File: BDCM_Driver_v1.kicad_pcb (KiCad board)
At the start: 4 copper layers, 32 x 33 mm, 38 parts, among them J1 OUT_{A}, J2 Encoder, J3 ST-Link, J4 Power, J5 I^{2}C, J6 Encoder, J7 OUT_{B}, SW1 RST, U1 STM32C011F4Px, U2 TB67H450FNG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

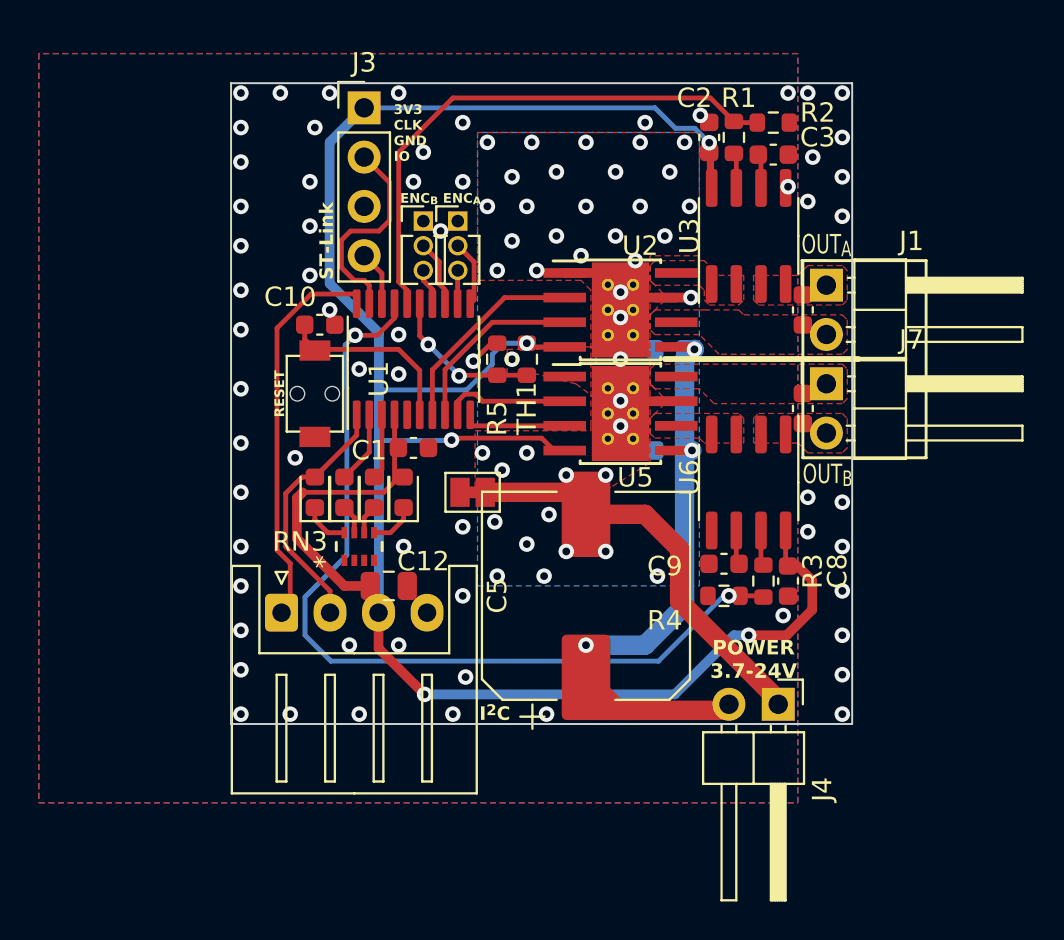
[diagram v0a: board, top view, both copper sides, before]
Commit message: ver2.0, change driver IC
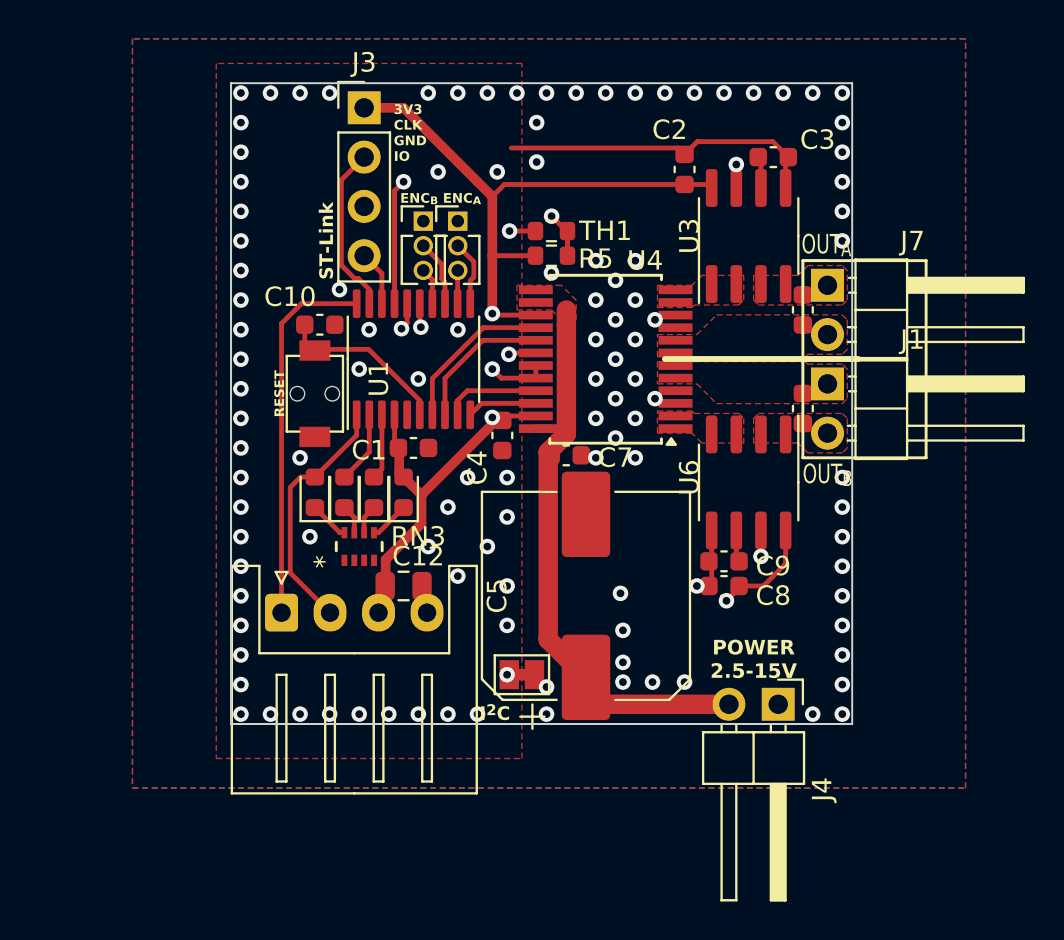
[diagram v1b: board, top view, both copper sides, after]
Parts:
- removed R1, R3: 5.1k, Resistor_SMD:R_0603_1608Metric
- removed R2, R4: 10k, Resistor_SMD:R_0603_1608Metric
- removed U2, U5: TB67H450FNG, Package_SO:Texas_HTSOP-8-1EP_3.9x4.9mm_P1.27mm_EP2.95x4.9mm_Mask2.4x3.1mm_ThermalVias
- added U4: TB6612FNG, Package_SO:SSOP-24_5.3x8.2mm_P0.65mm, F.Cu at (166.4, 122.2)
- C4, C7: moved to F.Cu
- moved JP3 9.74 mm to (162.1, 138.4)
- moved C4 8.66 mm to (161.0, 126.1), turned to -90 degrees
- moved C7 7.63 mm to (164.3, 127.1), turned to 0 degrees
- moved R5 7.17 mm to (163.6, 115.6), turned to 180 degrees
- moved TH1 5.48 mm to (163.6, 116.8), turned to 0 degrees
- moved J1 5.09 mm to (177.8, 123.4)
- moved C11 5.08 mm to (176.5, 119.6)
- moved C6 5.08 mm to (176.5, 124.7)
- moved J7 5.08 mm to (177.8, 118.4)
- moved C8 3.31 mm to (172.5, 133.9), turned to 180 degrees
- moved C2 2.08 mm to (170.4, 112.4)
- moved C12 0.76 mm to (156.0, 133.9)
- moved C3 0.13 mm to (175.0, 111.8)
- moved C9 0.13 mm to (172.5, 132.6)
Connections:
- C11 pad 1: OUT_B_{2} -> OUT_B_{1}'
- C11 pad 2: OUT_B_{1}' -> OUT_B_{2}
- C4 pad 1: Vdrive -> +3V3
- C4 pad 2: GNDPWR -> GND
- C6 pad 1: OUT_A_{2}' -> OUT_A_{2}
- C6 pad 2: OUT_A_{1} -> OUT_A_{1}'
- J1 pad 1: OUT_A_{2}' -> OUT_A_{2}
- J1 pad 2: OUT_A_{1} -> OUT_A_{1}'
- J7 pad 1: OUT_B_{2} -> OUT_B_{1}'
- J7 pad 2: OUT_B_{1}' -> OUT_B_{2}
- U1 pad 10: PWM_{2A} -> PWM_{1B}
- U1 pad 7: PWM_{1B} -> PWM_{2B}
- U1 pad 8: PWM_{1A} -> PWM_{2A}
- U1 pad 9: PWM_{2B} -> PWM_{1A}
- U3 pad 1: OUT_A_{2} -> OUT_B_{1}
- U3 pad 2: OUT_A_{2} -> OUT_B_{1}
- U3 pad 3: OUT_A_{2}' -> OUT_B_{1}'
- U3 pad 4: OUT_A_{2}' -> OUT_B_{1}'
- U3 pad 7: Net-(U3-VIOUT) -> Current_{2}
- U6 pad 1: OUT_B_{1}' -> OUT_A_{1}'
- U6 pad 2: OUT_B_{1}' -> OUT_A_{1}'
- U6 pad 3: OUT_B_{1} -> OUT_A_{1}
- U6 pad 4: OUT_B_{1} -> OUT_A_{1}
- U6 pad 7: Net-(U6-VIOUT) -> Current_{1}
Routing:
- net GND: track 1.90 -> 40.3 mm, vias 38 -> 41
- net +3V3: track 120.3 -> 83.8 mm, vias 5 -> 4
- net GNDPWR: track 29.6 -> 0.00 mm, vias 67 -> 74
- net Current_{2}: track 45.3 -> 26.1 mm
- net PWM_{1B}: track 10.7 -> 3.62 mm
- net TEMP: track 8.06 -> 12.7 mm
- net Vdrive: track 33.6 -> 28.9 mm, vias 3 -> 0
- net PWM_{1A}: track 9.51 -> 4.98 mm
- net Current_{1}: track 28.1 -> 31.5 mm, vias 0 -> 2
- net PWM_{2A}: track 4.86 -> 7.37 mm
- net SWDCLK: track 10.9 -> 8.75 mm
- net Net-(U3-VIOUT): track 1.83 -> 0.00 mm
- net Net-(U6-VIOUT): track 1.83 -> 0.00 mm
- net PWM_{2B}: track 6.51 -> 8.29 mm
- net I^{2}C_{SCL}: track 20.5 -> 19.2 mm
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- added copper zone on In1.Cu, net GND
- added copper zone on F.Cu, net OUT_A_{1}'
- added copper zone on F.Cu, net Vdrive
- removed copper zone on B.Cu, net GND
- removed copper zone on F.Cu, net OUT_A_{2}'
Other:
- board text added: "BDCM_Driver_v2.0 2024-12-07 2.5-15V/3.2A_{peak}"
- board text added: "POWER 2.5-15V"
- board text removed: "BDCM_Driver_v1.0 2024-06-01"
- board text removed: "POWER 3.7-24V"

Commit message: v2 manifactured
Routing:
- net GND: track 40.3 -> 44.1 mm
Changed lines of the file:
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@@
 		(tags "resistor")
 		(property "Reference" "R5"
-			(at -2.286 -1.43 360)
+			(at -2.286 -1.43 0)
 			(layer "F.SilkS")
 			(effects
@@
 		)
 		(property "Value" "10k"
-			(at 0 1.43 360)
+			(at 0 1.43 0)
 			(layer "F.Fab")
 			(effects
@@
 		)
 		(fp_text user "${REFERENCE}"
-			(at 0 0 360)
+			(at 0 0 0)
 			(layer "F.Fab")
 			(effects
@@
 		(tags "SSOP 0.65")
 		(property "Reference" "U4"
-			(at -2.032 5.08 360)
+			(at -2.032 5.08 0)
 			(layer "F.SilkS")
 			(effects
@@
 		)
 		(property "Value" "TB6612FNG"
-			(at 0 5.25 360)
+			(at 0 5.25 0)
 			(layer "F.Fab")
 			(effects
@@
 		)
 		(fp_text user "${REFERENCE}"
-			(at 0 0 360)
+			(at 0 0 0)
 			(layer "F.Fab")
 			(effects
@@
 		(tags "capacitor")
 		(property "Reference" "C2"
-			(at 2.032 -0.762 360)
+			(at 2.032 -0.762 0)
 			(layer "F.SilkS")
 			(effects
@@
 		(tags "capacitor")
 		(property "Reference" "C7"
-			(at 2.54 0.127 360)
+			(at 2.54 0.127 0)
 			(layer "F.SilkS")
 			(effects
@@
 		)
 		(property "Value" "0.1u"
-			(at 0 1.43 360)
+			(at 0 1.43 0)
 			(layer "F.Fab")
 			(effects
@@
 		)
 		(fp_text user "${REFERENCE}"
-			(at 0 0 360)
+			(at 0 0 0)
 			(layer "F.Fab")
 			(effects
@@
 		(tags "capacitor")
 		(property "Reference" "C8"
-			(at -2.54 -0.508 360)
+			(at -2.54 -0.508 0)
 			(layer "F.SilkS")
 			(effects
@@
 		)
 		(property "Value" "0.1u"
-			(at 0 1.43 360)
+			(at 0 1.43 0)
 			(layer "F.Fab")
 			(effects
@@
 		)
 		(property "Footprint" "Capacitor_SMD:C_0603_1608Metric"
-			(at 0 0 360)
+			(at 0 0 0)
 			(layer "F.Fab")
 			(hide yes)
@@
 		)
 		(property "Datasheet" ""
-			(at 0 0 360)
+			(at 0 0 0)
 			(layer "F.Fab")
 			(hide yes)
@@
 		)
 		(property "Description" ""
-			(at 0 0 360)
+			(at 0 0 0)
 			(layer "F.Fab")
 			(hide yes)
@@
 		)
 		(fp_text user "${REFERENCE}"
-			(at 0 0 360)
+			(at 0 0 0)
 			(layer "F.Fab")
 			(effects
@@
 	)
 	(segment
+		(start 156.139 125.0365)
+		(end 156.139 124.285397)
+		(width 0.25)
+		(layer "F.Cu")
+		(net 2)
+	)
+	(segment
+		(start 156.139 124.285397)
+		(end 155.563301 123.709698)
+		(width 0.25)
+		(layer "F.Cu")
+		(net 2)
+	)
+	(segment
 		(start 170.103 111.289)
 		(end 161.507 111.289)
@@
 	)
 	(segment
+		(start 156.139 125.773999)
+		(end 157.111001 126.746)
+		(width 0.25)
+		(layer "F.Cu")
+		(net 2)
+	)
+	(segment
 		(start 171.094 110.96)
 		(end 170.434 111.62)
@@
 	)
 	(segment
+		(start 157.111001 126.746)
+		(end 157.239 126.746)
+		(width 0.25)
+		(layer "F.Cu")
+		(net 2)
+	)
+	(segment
 		(start 175.641 111.9)
 		(end 175.781 111.76)
@@
 		(net 2)
 	)
+	(segment
+		(start 156.139 125.0365)
+		(end 156.139 125.773999)
+		(width 0.25)
+		(layer "F.Cu")
+		(net 2)
+	)
 	(via
 		(at 160.274 131.826)
@@
 		(polygon
 			(pts
-				(xy 169.037 119.507) (xy 170.815 119.507) (xy 170.942 119.38) (xy 173.228 119.38) (xy 173.482 119.126)
-				(xy 173.482 117.856) (xy 171.323 117.856) (xy 170.815 118.364) (xy 169.037 118.364)
+				(xy 169.037 119.507) (xy 173.101 119.507) (xy 173.482 119.126) (xy 173.482 117.856) (xy 171.323 117.856)
+				(xy 170.815 118.364) (xy 169.037 118.364)
 			)
 		)
@@
 		(polygon
 			(pts
-				(xy 169.037 124.841) (xy 170.815 124.841) (xy 170.942 124.968) (xy 173.228 124.968) (xy 173.482 125.222)
-				(xy 173.482 126.492) (xy 171.323 126.492) (xy 170.815 125.984) (xy 169.037 125.984)
+				(xy 169.037 124.841) (xy 173.101 124.841) (xy 173.482 125.222) (xy 173.482 126.492) (xy 171.323 126.492)
+				(xy 170.815 125.984) (xy 169.037 125.984)
 			)
 		)
@@
 		(hatch edge 0.5)
 		(priority 2)
-		(connect_pads yes
+		(connect_pads
 			(clearance 0)
 		)
@@
 		(filled_areas_thickness no)
 		(fill yes
+			(mode hatch)
 			(thermal_gap 0.5)
 			(thermal_bridge_width 0.5)
+			(hatch_thickness 0.5)
+			(hatch_gap 0.5)
+			(hatch_orientation 45)
+			(hatch_border_algorithm hatch_thickness)
+			(hatch_min_hole_area 0.3)
 		)
 		(polygon
@@
 			)
 		)
+	)
+	(zone
+		(net 0)
+		(net_name "")
+		(layers "F.Cu" "In1.Cu" "In2.Cu" "B.Cu")
+		(hatch edge 0.5)
+		(connect_pads
+			(clearance 0)
+		)
+		(min_thickness 0.25)
+		(filled_areas_thickness no)
+		(keepout
+			(tracks allowed)
+			(vias allowed)
+			(pads allowed)
+			(copperpour not_allowed)
+			(footprints allowed)
+		)
+		(fill
+			(thermal_gap 0.5)
+			(thermal_bridge_width 0.5)
+		)
+		(polygon
+			(pts
+				(xy 171.196 129.921) (xy 176.276 129.921) (xy 176.276 126.619) (xy 171.196 126.619)
+			)
+		)
+	)
+	(zone
+		(net 0)
+		(net_name "")
+		(layers "F.Cu" "In1.Cu" "In2.Cu" "B.Cu")
+		(hatch edge 0.5)
+		(connect_pads
+			(clearance 0)
+		)
+		(min_thickness 0.25)
+		(filled_areas_thickness no)
+		(keepout
+			(tracks allowed)
+			(vias allowed)
+			(pads allowed)
+			(copperpour not_allowed)
+			(footprints allowed)
+		)
+		(fill
+			(thermal_gap 0.5)
+			(thermal_bridge_width 0.5)
+		)
+		(polygon
+			(pts
+				(xy 171.196 117.729) (xy 176.276 117.729) (xy 176.276 114.427) (xy 171.196 114.427)
+			)
+		)
